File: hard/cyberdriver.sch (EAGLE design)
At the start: 1 part

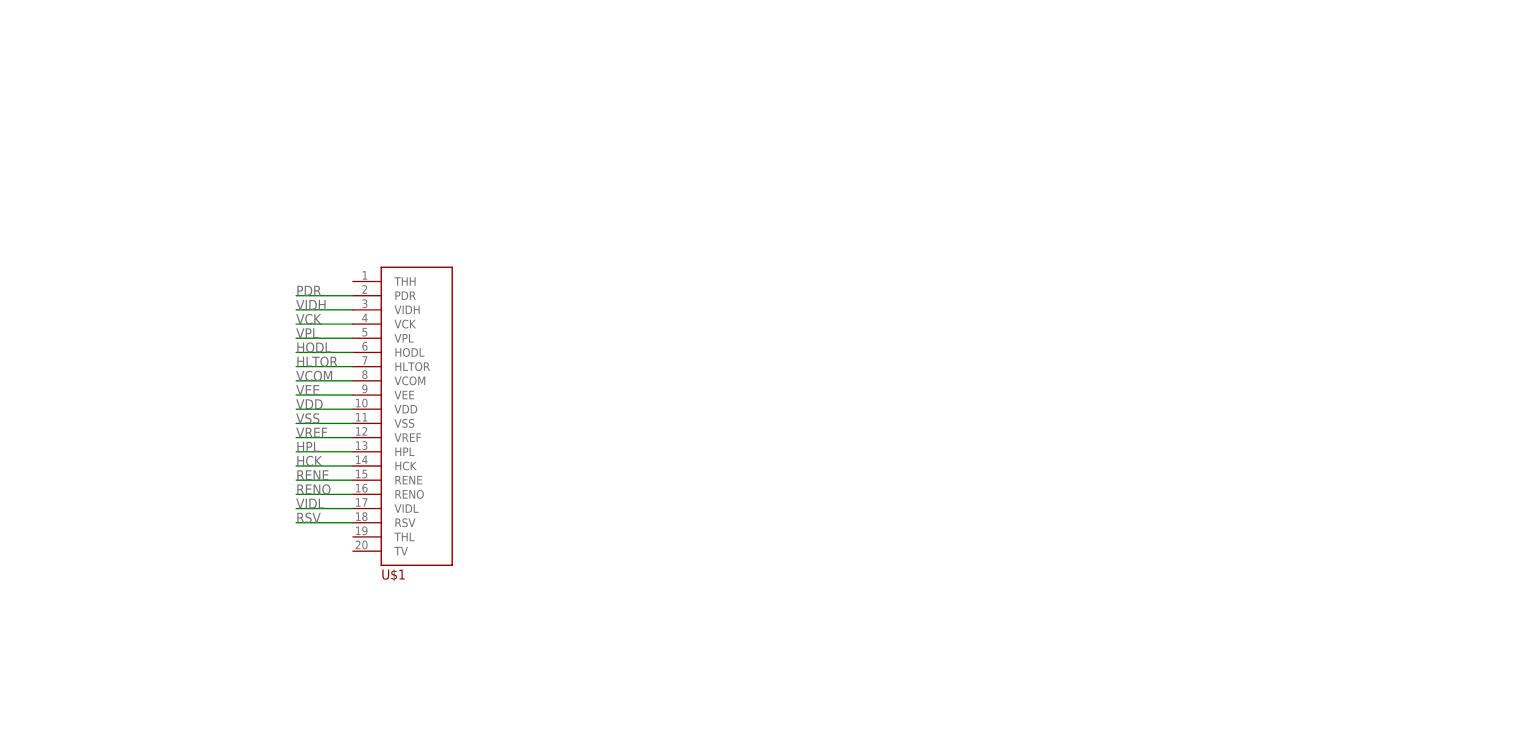
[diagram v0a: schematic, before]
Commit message: Display Power Regs Added
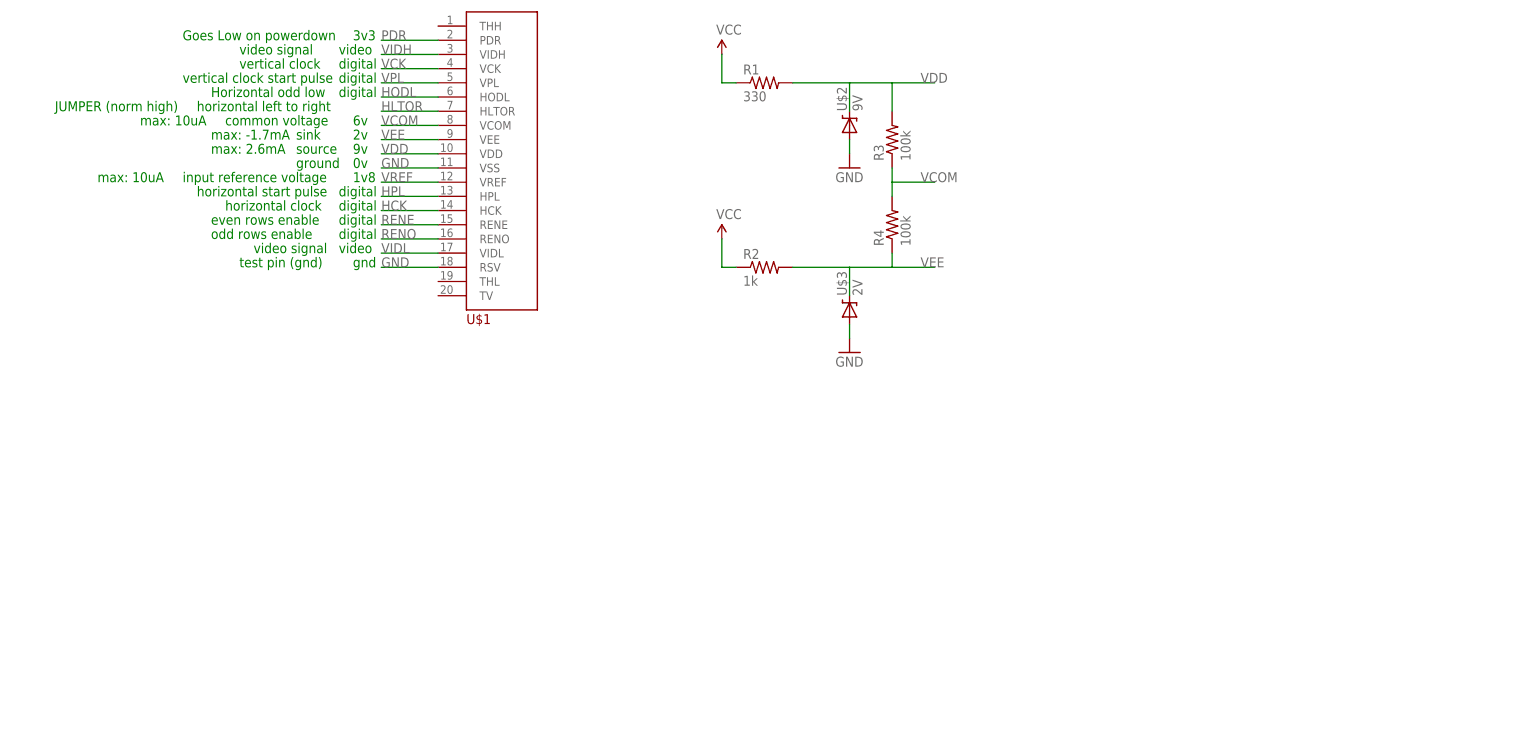
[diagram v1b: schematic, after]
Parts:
- added R1: 330, cyberdriver:RESISTOR0603-RES
- added R2: 1k, cyberdriver:RESISTOR0603-RES
- added R3, R4: 100k, cyberdriver:RESISTOR0805-RES
- added U$2: 9V, cyberdriver:DIODE-ZENER-BZT52
- added U$3: 2V, cyberdriver:DIODE-ZENER-BZT52
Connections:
- removed net RSV: U$1.RSV
- removed net VSS: U$1.VSS
- new net GND: U$1.RSV, U$1.VSS, U$2.A, U$3.A
- new net VCC: R1.1, R2.1
- net VCOM: now also R3.1, R4.2
- net VDD: now also R1.2, R3.2, U$2.C
- net VEE: now also R2.2, R4.1, U$3.C
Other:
- note added: "0v"
- note added: "1v8"
- note added: "2v"
- note added: "3v3"
- note added: "6v"
- note added: "9v"
- note added: "Goes Low on powerdown"
- note added: "Horizontal odd low"
- note added: "JUMPER (norm high)"
- note added: "common voltage"
- note added: "digital"
- note added: "even rows enable"
- note added: "gnd"
- note added: "ground"
- note added: "horizontal clock"
- note added: "horizontal left to right"
- note added: "horizontal start pulse"
- note added: "input reference voltage"
- note added: "max: -1.7mA"
- note added: "max: 10uA"
- note added: "max: 2.6mA"
- note added: "odd rows enable"
- note added: "sink"
- note added: "source"
- note added: "test pin (gnd)"
- note added: "vertical clock"
- note added: "vertical clock start pulse"
- note added: "video"
- note added: "video signal"
- moved on the sheet: U$1

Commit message: Changes to Schematic and New Board
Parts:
- added C1, C2: (no value), cyberdriver:CAP_POLC
- added C3: (no value), cyberdriver:CAP_POL1206
- added IC1: OPAMP-DUALU, cyberdriver:OPAMP-DUALU
- added ICSP: AVR_SPI_PRG_6NS, cyberdriver:AVR_SPI_PRG_6NS
- added JP1: M02PTH, cyberdriver:M02PTH
- added L1: 33uH, cyberdriver:INDUCTORBOURNS_SRN6045
- added LED1: (no value), cyberdriver:LED1206
- added Q1: MOSFET-NCHANNELBSS123LT1G, cyberdriver:MOSFET-NCHANNELBSS123LT1G
- added R10, R11, R12, R13, R14, R15, R16, R17, R5: (no value), cyberdriver:RESISTOR0805-RES
- added R6, R7, R8, R9: 10k, cyberdriver:RESISTOR0805-RES
- added SJ1: SOLDERJUMPERNO, cyberdriver:SOLDERJUMPERNO
- added U1: ATTINY2313A, cyberdriver:ATTINY2313A
- added UART: (no value), cyberdriver:M04PTH
- added Y1: (no value), cyberdriver:CRYSTAL5X3
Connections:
- removed net HODL: U$1.HODL
- removed net VCK: U$1.VCK
- removed net VPL: U$1.VPL
- new net 12V: C2.+, C3.+, IC1A.V+, L1.2, R1.1, R2.1
- new net AO0: R13.1, U1.PD2/INT0
- new net AO1: R12.1, U1.PD3/INT1
- new net AO2: R11.1, U1.PD4
- new net AO3: R10.2, U1.PD6
- new net A_VID: IC1B.+IN, R10.1, R14.2
- new net HODL/MOSI: ICSP.4, U$1.HODL, U1.PB5/MOSI/SDA/DI
- new net N$1: U1.PA0/XTAL1, Y1.2
- new net N$11: R13.2, R16.1, R17.2
- new net N$2: U1.PA1/XTAL2, Y1.1
- new net N$3: C1.+, L1.1, Q1.D
- new net N$5: IC1A.-IN, R6.1, R7.2
- new net N$6: R11.2, R14.1, R15.2
- new net N$7: IC1B.-IN, R8.2, R9.2
- new net N$9: R12.2, R15.1, R16.2
- new net PS_FB: U1.PB0
- new net PS_PWM: Q1.G, U1.PD5
- new net RST: ICSP.5, R5.1, SJ1.2, U1.PA2/!RESET
- new net RXD: U1.PD0/RXD, UART.2
- new net TXD: U1.PD1/TXD, UART.3
- new net VCK/SCK: ICSP.3, U$1.VCK, U1.PB7/SCK/SCL
- new net VPL/MISO: ICSP.1, U$1.VPL, U1.PB6/MISO/DO
- net GND: now also C1.-, C2.-, C3.-, IC1A.V-, ICSP.6, JP1.1, LED1.C, Q1.S, R17.1, SJ1.1, U1.GND, UART.1
- net HCK: now also U1.PB3
- net HPL: now also U1.PB4
- net RENE: now also U1.PB2
- net RENO: now also U1.PB1
- net VCC: now also ICSP.2, JP1.2, LED1.A, R5.2, U1.VCC, UART.4; no longer R1.1, R2.1
- net VDD: now also IC1A.+IN
- net VEE: now also R8.1
- net VIDH: now also IC1A.OUT, R6.2
- net VIDL: now also IC1B.OUT, R7.1, R9.1
